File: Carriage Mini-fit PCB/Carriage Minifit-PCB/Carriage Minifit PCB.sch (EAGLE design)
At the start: 3 parts, among them J1 39281063, X1 JST-XH-02-PIN-LONG-PAD, X2 TERMINAL-BLOCK-3.5MM-4-PIN-LO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

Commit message: Added Logo
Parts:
- added U$1, U$2: FWLOGO_SMALL_FOOTPRINT, FracktalWorks_Eagle_Library:FWLOGO_SMALL_FOOTPRINT
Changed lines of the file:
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@@
 <layer number="56" name="wert" color="7" fill="1" visible="no" active="no"/>
 <layer number="57" name="tCAD" color="7" fill="1" visible="no" active="no"/>
+<layer number="59" name="tCarbon" color="7" fill="1" visible="no" active="no"/>
+<layer number="60" name="bCarbon" color="7" fill="1" visible="no" active="no"/>
 <layer number="88" name="SimResults" color="9" fill="1" visible="yes" active="yes"/>
 <layer number="89" name="SimProbes" color="9" fill="1" visible="yes" active="yes"/>
@@
 <layer number="112" name="tSilk" color="7" fill="1" visible="yes" active="yes"/>
 <layer number="113" name="IDFDebug" color="4" fill="1" visible="yes" active="yes"/>
+<layer number="114" name="Badge_Outline" color="7" fill="1" visible="yes" active="yes"/>
+<layer number="115" name="ReferenceISLANDS" color="7" fill="1" visible="yes" active="yes"/>
 <layer number="116" name="Patch_BOT" color="9" fill="4" visible="yes" active="yes"/>
+<layer number="118" name="Rect_Pads" color="7" fill="1" visible="yes" active="yes"/>
 <layer number="121" name="_tsilk" color="7" fill="1" visible="yes" active="yes"/>
 <layer number="122" name="_bsilk" color="7" fill="1" visible="yes" active="yes"/>
@@
 <layer number="127" name="_tValues" color="7" fill="1" visible="yes" active="yes"/>
 <layer number="128" name="_bValues" color="7" fill="1" visible="yes" active="yes"/>
+<layer number="129" name="Mask" color="7" fill="1" visible="yes" active="yes"/>
 <layer number="131" name="tAdjust" color="7" fill="1" visible="yes" active="yes"/>
 <layer number="132" name="bAdjust" color="7" fill="1" visible="yes" active="yes"/>
@@
 <layer number="230" name="230bmp" color="7" fill="1" visible="yes" active="yes"/>
 <layer number="231" name="231bmp" color="7" fill="1" visible="yes" active="yes"/>
+<layer number="232" name="Eagle3D_PG2" color="7" fill="1" visible="yes" active="yes"/>
+<layer number="233" name="Eagle3D_PG3" color="7" fill="1" visible="yes" active="yes"/>
 <layer number="248" name="Housing" color="7" fill="1" visible="yes" active="yes"/>
 <layer number="249" name="Edge" color="7" fill="1" visible="yes" active="yes"/>
@@
 <layer number="251" name="SMDround" color="12" fill="11" visible="no" active="no"/>
 <layer number="254" name="cooling" color="7" fill="1" visible="yes" active="yes"/>
+<layer number="255" name="routoute" color="7" fill="1" visible="yes" active="yes"/>
 </layers>
 <schematic xreflabel="%F%N/%S.%C%R" xrefpart="/%S.%C%R">
@@
 <part name="X1" library="Rembrandt Electronics - JST XH Connectors v1-0" deviceset="JST-XH-02-PIN" device="-LONG-PAD"/>
 <part name="X2" library="Rembrandt Electronics - Terminal Block 3-5mm v1-0" deviceset="TERMINAL-BLOCK-3.5MM-4-PIN" device="-LONG-PAD"/>
+<part name="U$1" library="FracktalWorks_Eagle_Library" deviceset="FWLOGO_SMALL_FOOTPRINT" device=""/>
+<part name="U$2" library="FracktalWorks_Eagle_Library" deviceset="FWLOGO_SMALL_FOOTPRINT" device=""/>
 </parts>
 <sheets>

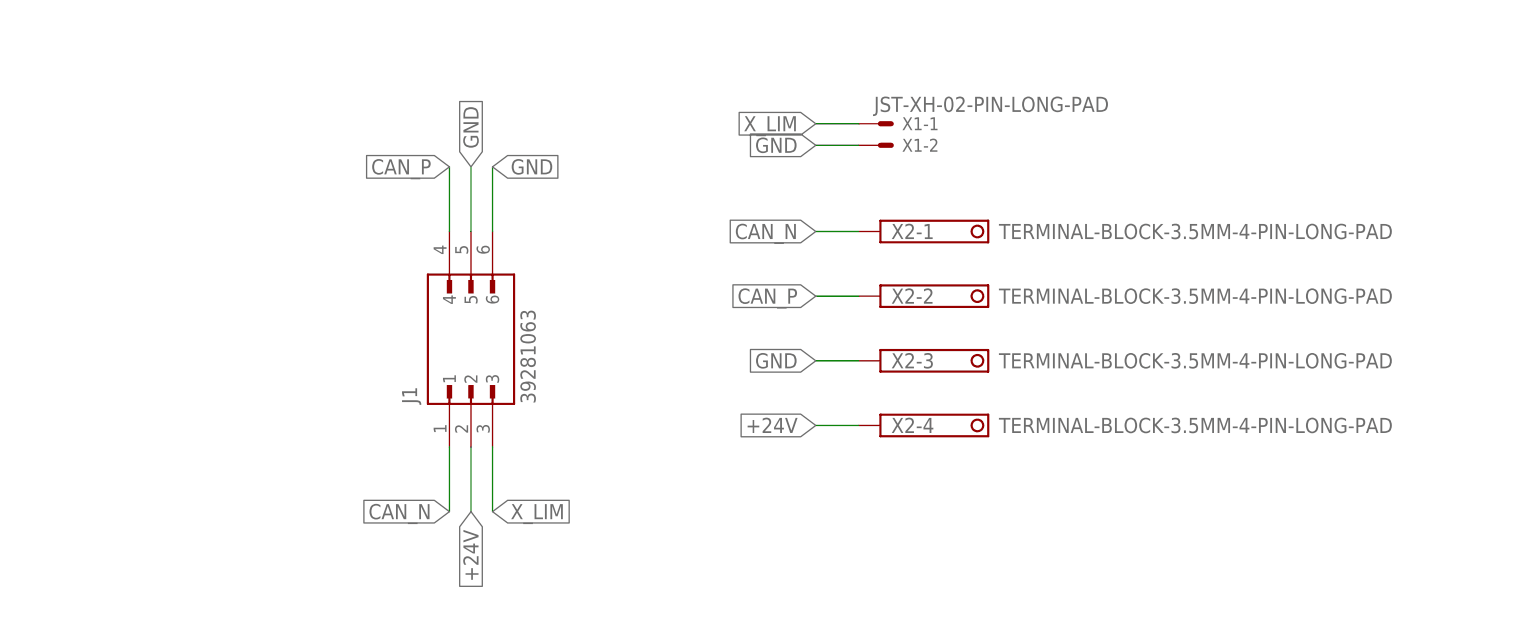
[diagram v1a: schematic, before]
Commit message: Updated Toolboard V2 and Carriage minifit boards specs
Toolboard and Carriage minifit board design,  gerber, BOMs, centroids and connector specifications have been updated here
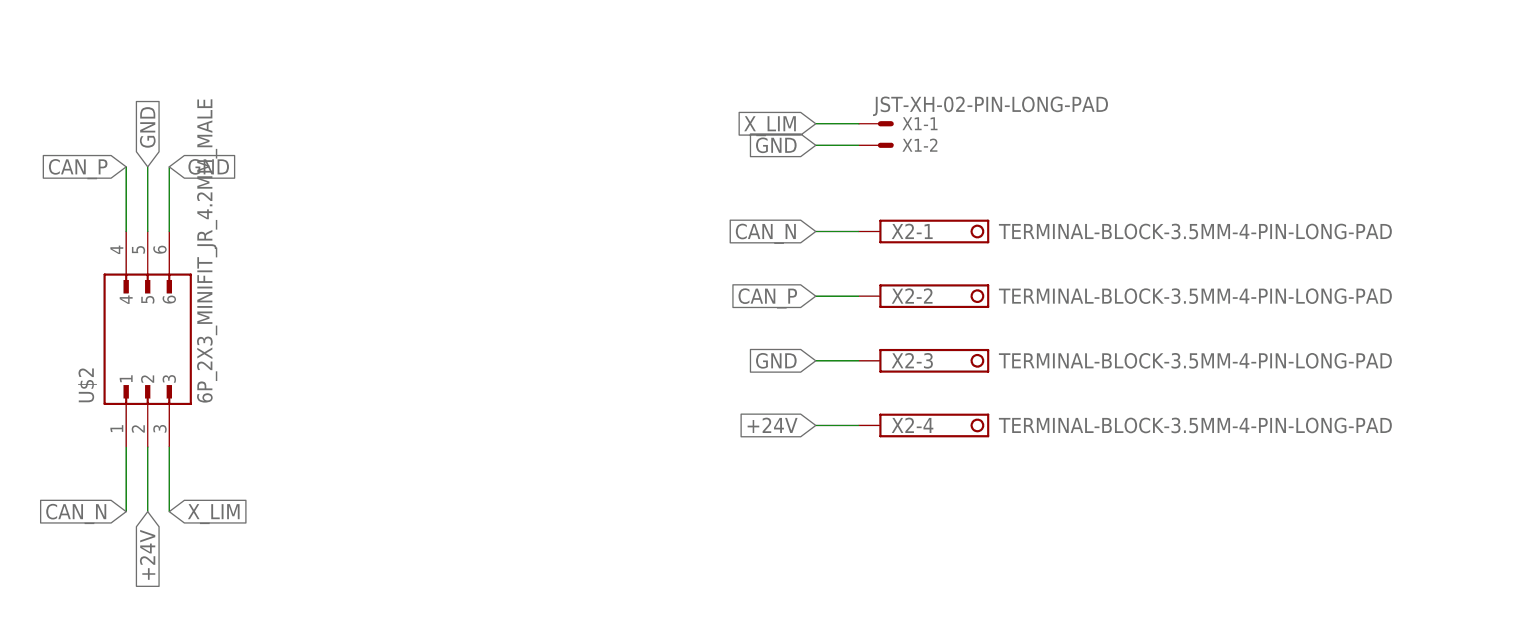
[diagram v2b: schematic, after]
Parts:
- removed J1: 39281063, Minifit Jr 2x3:39281063
- removed U$1: FWLOGO_SMALL_FOOTPRINT, FracktalWorks_Eagle_Library:FWLOGO_SMALL_FOOTPRINT
- U$2: value FWLOGO_SMALL_FOOTPRINT -> 6P_2X3_MINIFIT_JR_4.2MM_MALE; device FracktalWorks_Eagle_Library:FWLOGO_SMALL_FOOTPRINT -> 6P_2x3_Minifit_Jr_4.2mm_Male:6P_2X3_MINIFIT_JR_4.2MM_MALE
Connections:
- net +24V: now also U$2.2; no longer J1.2
- net CAN_N: now also U$2.1; no longer J1.1
- net CAN_P: now also U$2.4; no longer J1.4
- net GND: now also U$2.5, U$2.6; no longer J1.5, J1.6
- net X_LIM: now also U$2.3; no longer J1.3
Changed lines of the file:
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@@
 <layers>
 <layer number="1" name="Top" color="4" fill="1" visible="no" active="no"/>
+<layer number="2" name="Route2" color="16" fill="1" visible="no" active="no"/>
+<layer number="3" name="Route3" color="17" fill="1" visible="no" active="no"/>
+<layer number="4" name="Route4" color="18" fill="1" visible="no" active="no"/>
+<layer number="5" name="Route5" color="19" fill="1" visible="no" active="no"/>
+<layer number="6" name="Route6" color="25" fill="1" visible="no" active="no"/>
+<layer number="7" name="Route7" color="26" fill="1" visible="no" active="no"/>
+<layer number="8" name="Route8" color="27" fill="1" visible="no" active="no"/>
+<layer number="9" name="Route9" color="28" fill="1" visible="no" active="no"/>
+<layer number="10" name="Route10" color="29" fill="1" visible="no" active="no"/>
+<layer number="11" name="Route11" color="30" fill="1" visible="no" active="no"/>
+<layer number="12" name="Route12" color="20" fill="1" visible="no" active="no"/>
+<layer number="13" name="Route13" color="21" fill="1" visible="no" active="no"/>
+<layer number="14" name="Route14" color="22" fill="1" visible="no" active="no"/>
+<layer number="15" name="Route15" color="23" fill="1" visible="no" active="no"/>
 <layer number="16" name="Bottom" color="1" fill="1" visible="no" active="no"/>
 <layer number="17" name="Pads" color="2" fill="1" visible="no" active="no"/>
@@
 </classes>
 <parts>
-<part name="J1" library="Minifit Jr 2x3" deviceset="39281063" device=""/>
 <part name="X1" library="Rembrandt Electronics - JST XH Connectors v1-0" deviceset="JST-XH-02-PIN" device="-LONG-PAD"/>
 <part name="X2" library="Rembrandt Electronics - Terminal Block 3-5mm v1-0" deviceset="TERMINAL-BLOCK-3.5MM-4-PIN" device="-LONG-PAD"/>
-<part name="U$1" library="FracktalWorks_Eagle_Library" deviceset="FWLOGO_SMALL_FOOTPRINT" device=""/>
-<part name="U$2" library="FracktalWorks_Eagle_Library" deviceset="FWLOGO_SMALL_FOOTPRINT" device=""/>
+<part name="U$2" library="6P_2x3_Minifit_Jr_4.2mm_Male" deviceset="6P_2X3_MINIFIT_JR_4.2MM_MALE" device=""/>
 </parts>
 <sheets>
@@
 </plain>
 <instances>
-<instance part="J1" gate="G$1" x="40.64" y="38.1" smashed="yes" rot="R90">
-<attribute name="NAME" x="34.29" y="30.48" size="1.778" layer="95" rot="R90"/>
-<attribute name="VALUE" x="48.26" y="30.48" size="1.778" layer="96" rot="R90"/>
-</instance>
 <instance part="X1" gate="-2" x="88.9" y="60.96" smashed="yes">
 <attribute name="NAME" x="91.44" y="60.198" size="1.524" layer="95"/>
@@
 <attribute name="NAME" x="90.17" y="27.051" size="1.778" layer="95"/>
 <attribute name="VALUE" x="102.87" y="27.051" size="1.778" layer="96"/>
+</instance>
+<instance part="U$2" gate="G$1" x="2.54" y="38.1" smashed="yes" rot="R90">
+<attribute name="NAME" x="-3.81" y="30.48" size="1.778" layer="95" rot="R90"/>
+<attribute name="VALUE" x="10.16" y="30.48" size="1.778" layer="96" rot="R90"/>
 </instance>
 </instances>
@@
 <net name="+24V" class="0">
 <segment>
-<pinref part="J1" gate="G$1" pin="2"/>
-<wire x1="40.64" y1="25.4" x2="40.64" y2="17.78" width="0.1524" layer="91"/>
-<label x="40.64" y="17.78" size="1.778" layer="95" rot="R270" xref="yes"/>
-</segment>
-<segment>
 <pinref part="X2" gate="-4" pin="K"/>
 <wire x1="86.36" y1="27.94" x2="81.28" y2="27.94" width="0.1524" layer="91"/>
 <label x="81.28" y="27.94" size="1.778" layer="95" rot="R180" xref="yes"/>
 </segment>
+<segment>
+<wire x1="2.54" y1="25.4" x2="2.54" y2="17.78" width="0.1524" layer="91"/>
+<label x="2.54" y="17.78" size="1.778" layer="95" rot="R270" xref="yes"/>
+<pinref part="U$2" gate="G$1" pin="2"/>
+</segment>
 </net>
 <net name="GND" class="0">
-<segment>
-<pinref part="J1" gate="G$1" pin="5"/>
-<wire x1="40.64" y1="50.8" x2="40.64" y2="58.42" width="0.1524" layer="91"/>
-<label x="40.64" y="58.42" size="1.778" layer="95" rot="R90" xref="yes"/>
-</segment>
-<segment>
-<pinref part="J1" gate="G$1" pin="6"/>
-<wire x1="43.18" y1="50.8" x2="43.18" y2="58.42" width="0.1524" layer="91"/>
-<label x="43.18" y="58.42" size="1.778" layer="95" xref="yes"/>
-</segment>
 <segment>
 <pinref part="X1" gate="-2" pin="S"/>
@@
 <label x="81.28" y="35.56" size="1.778" layer="95" rot="R180" xref="yes"/>
 </segment>
+<segment>
+<wire x1="2.54" y1="50.8" x2="2.54" y2="58.42" width="0.1524" layer="91"/>
+<label x="2.54" y="58.42" size="1.778" layer="95" rot="R90" xref="yes"/>
+<pinref part="U$2" gate="G$1" pin="5"/>
+</segment>
+<segment>
+<wire x1="5.08" y1="50.8" x2="5.08" y2="58.42" width="0.1524" layer="91"/>
+<label x="5.08" y="58.42" size="1.778" layer="95" xref="yes"/>
+<pinref part="U$2" gate="G$1" pin="6"/>
+</segment>
 </net>
 <net name="X_LIM" class="0">
-<segment>
-<pinref part="J1" gate="G$1" pin="3"/>
-<wire x1="43.18" y1="25.4" x2="43.18" y2="17.78" width="0.1524" layer="91"/>
-<label x="43.18" y="17.78" size="1.778" layer="95" xref="yes"/>
-</segment>
 <segment>
 <pinref part="X1" gate="-1" pin="S"/>
@@
 <label x="81.28" y="63.5" size="1.778" layer="95" rot="R180" xref="yes"/>
 </segment>
+<segment>
+<wire x1="5.08" y1="25.4" x2="5.08" y2="17.78" width="0.1524" layer="91"/>
+<label x="5.08" y="17.78" size="1.778" layer="95" xref="yes"/>
+<pinref part="U$2" gate="G$1" pin="3"/>
+</segment>
 </net>
 <net name="CAN_P" class="1">
-<segment>
-<pinref part="J1" gate="G$1" pin="4"/>
-<wire x1="38.1" y1="50.8" x2="38.1" y2="58.42" width="0.1524" layer="91"/>
-<label x="38.1" y="58.42" size="1.778" layer="95" rot="R180" xref="yes"/>
-</segment>
 <segment>
 <pinref part="X2" gate="-2" pin="K"/>
@@
 <label x="81.28" y="43.18" size="1.778" layer="95" rot="R180" xref="yes"/>
 </segment>
+<segment>
+<wire x1="0" y1="50.8" x2="0" y2="58.42" width="0.1524" layer="91"/>
+<label x="0" y="58.42" size="1.778" layer="95" rot="R180" xref="yes"/>
+<pinref part="U$2" gate="G$1" pin="4"/>
+</segment>
 </net>
 <net name="CAN_N" class="1">
-<segment>
-<pinref part="J1" gate="G$1" pin="1"/>
-<wire x1="38.1" y1="25.4" x2="38.1" y2="17.78" width="0.1524" layer="91"/>
-<label x="38.1" y="17.78" size="1.778" layer="95" rot="R180" xref="yes"/>
-</segment>
 <segment>
 <pinref part="X2" gate="-1" pin="K"/>
@@
 <label x="81.28" y="50.8" size="1.778" layer="95" rot="R180" xref="yes"/>
 </segment>
-</net>
+<segment>
+<wire x1="0" y1="25.4" x2="0" y2="17.78" width="0.1524" layer="91"/>
+<label x="0" y="17.78" size="1.778" layer="95" rot="R180" xref="yes"/>
+<pinref part="U$2" gate="G$1" pin="1"/>
+</segment>
+</net>
